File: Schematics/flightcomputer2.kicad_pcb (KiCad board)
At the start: 4 copper layers, 80 x 80 mm, 105 parts, among them J1 Microsemi_FlashPro-JTAG-10, J10 Pyro, J2 Pyro, J4 Drouge, J5 Conn_01x05_Pin, J6 Conn_01x05_Pin, J7 Conn_Coaxial_Small, J8 Micro_SD_Card, J9 USB_C_Receptacle_USB2.0_16P, Q1 IRLML2502TRPBF, Q2 IRLML2502TRPBF, Q3 BC817, Q4 IRLML2502TRPBF, Q6 Q_PMOS_GSD, SW1 SAMZO G4R0015010, SW2 SAMZO G4R0015010, U1 STM32F405RGT6, U2 SN65HVD230, U3 PowerIn, U4 LDL1117-3.3, U5 RFM95W-915S2, U6 Bosch BMP388, U7 LSM6DS3TR-C, U8 W25Q128JVP, U9 H3LIS331DL, Y1 8mhz

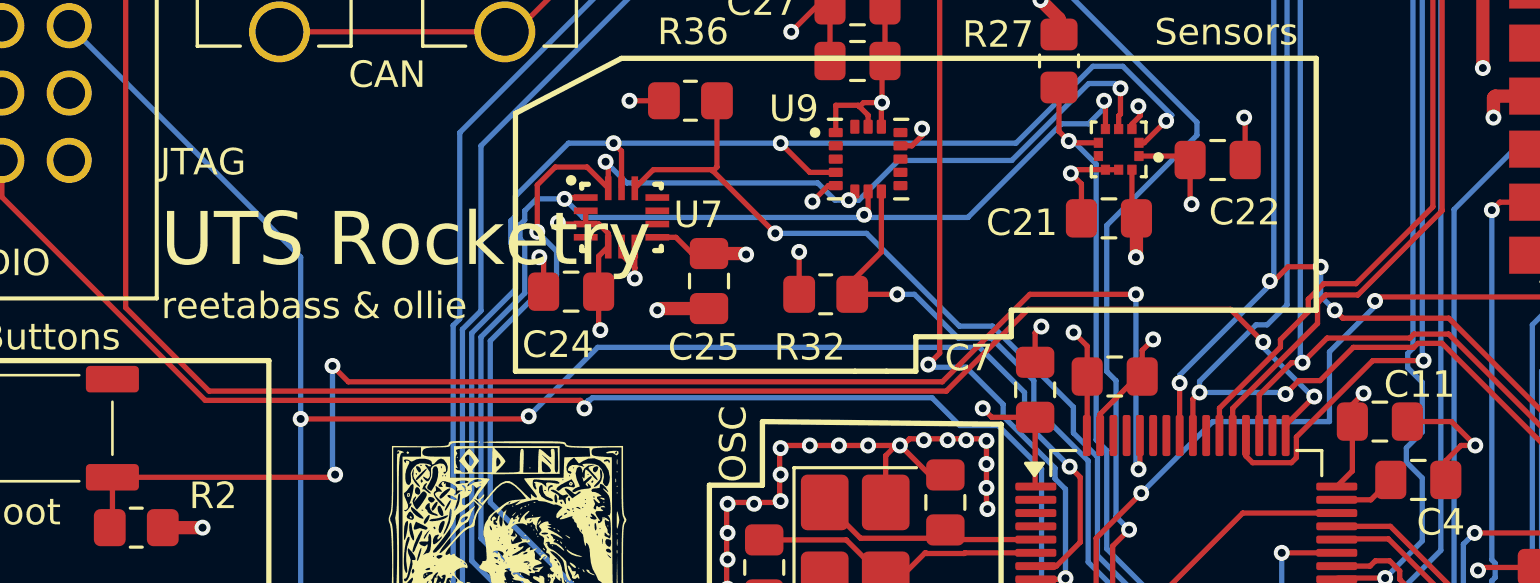
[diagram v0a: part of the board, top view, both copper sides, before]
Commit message: ran dmf check fixed some things
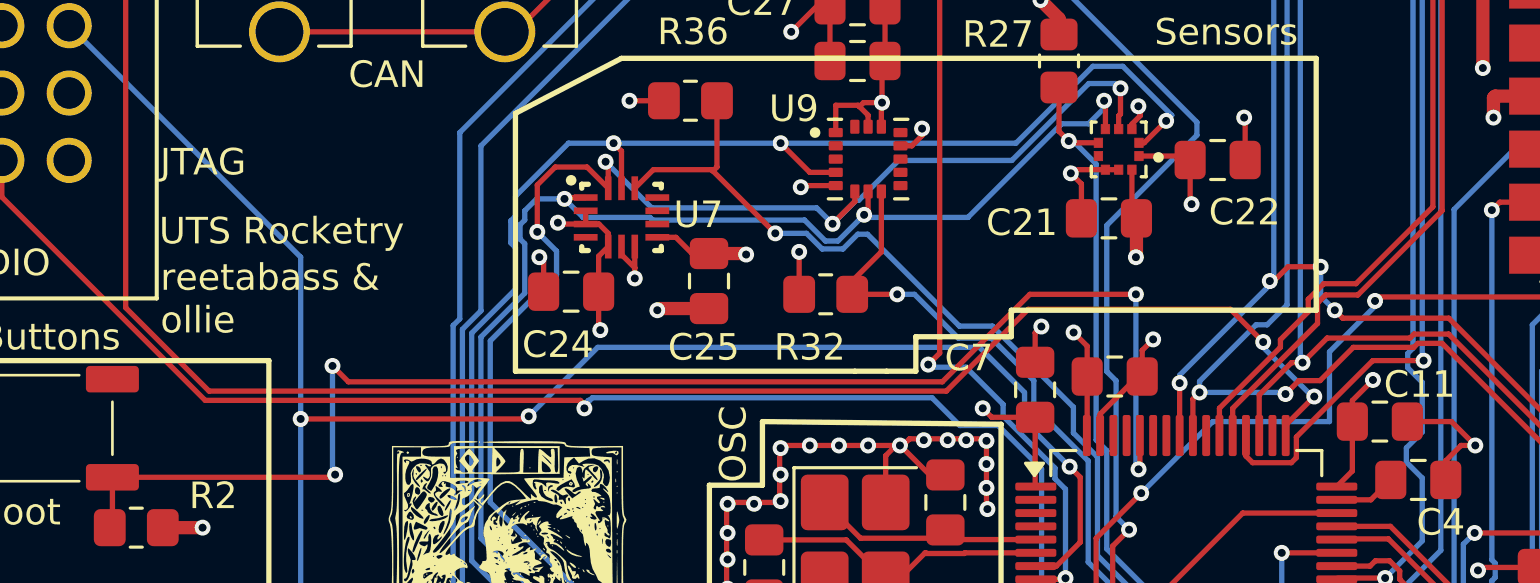
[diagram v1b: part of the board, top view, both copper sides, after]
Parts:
- R30: value 40k -> 47k
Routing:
- net /Accelerometer/Accelerometer_MOSI: track 75.4 -> 77.4 mm
- net /Accelerometer/Accelerometer_MIS0: track 73.1 -> 73.8 mm
- net +3.3V: track 107.7 -> 108.4 mm
